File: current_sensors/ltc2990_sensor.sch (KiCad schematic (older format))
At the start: 14 parts

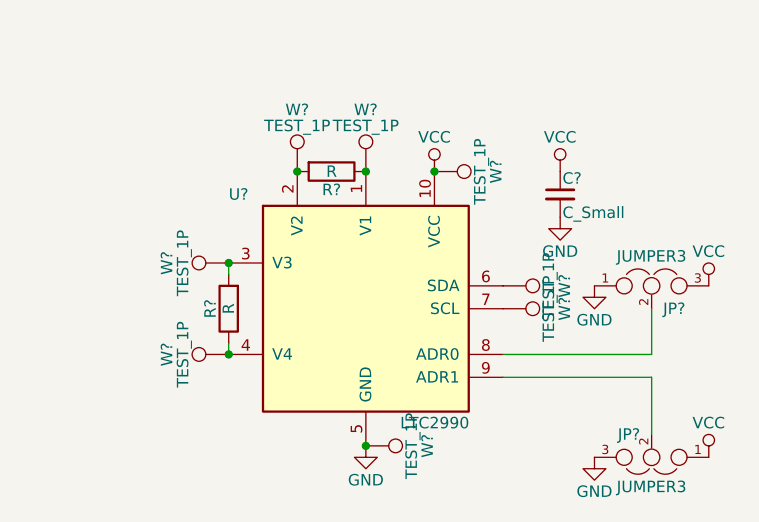
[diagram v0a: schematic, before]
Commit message: Made LTC2990 current sensor addon, untested
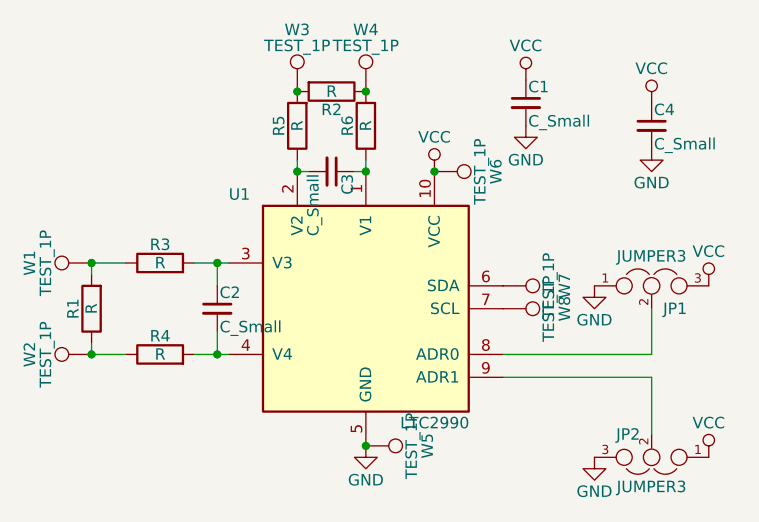
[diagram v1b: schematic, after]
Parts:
- added C2, C3, C4: C_Small, Capacitors_SMD:C_0603, symbol C_Small
- added R3, R4, R5, R6: R, Resistors_SMD:R_0603, symbol R
- C1: renamed from C?; footprint (none) -> Capacitors_SMD:C_0603
- JP1, JP2: renamed from JP?; footprint (none) -> Connect:GS3
- R1, R2: renamed from R?; footprint (none) -> Resistors_SMD:R_2512_HandSoldering
- U1: renamed from U?; footprint (none) -> Housings_SSOP:MSOP-10_3x3mm_Pitch0.5mm
- W1, W2, W3, W4: renamed from W?; footprint (none) -> Measurement_Points:Measurement_Point_Square-SMD-Pad_Big
- W5, W6, W7, W8: renamed from W?; footprint (none) -> Measurement_Points:Measurement_Point_Square-SMD-Pad_Small
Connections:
- net GND: now also C4.2
- net VCC: now also C4.1
- net at R2.1, W4.1: now also R6.2; no longer U1.1 (V1)
- net at R2.2, W3.1: now also R5.2; no longer U1.2 (V2)
- net at R1.2, W1.1: now also R3.1; no longer U1.3 (V3)
- net at R1.1, W2.1: now also R4.1; no longer U1.4 (V4)
- new net: C3.1, R6.1, U1.1 (V1)
- new net: C3.2, R5.1, U1.2 (V2)
- new net: C2.1, R3.2, U1.3 (V3)
- new net: C2.2, R4.2, U1.4 (V4)
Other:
- moved on the sheet: C1, R1, R2, W1, W2, W3, W4

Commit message: Added ground pads to current sensor
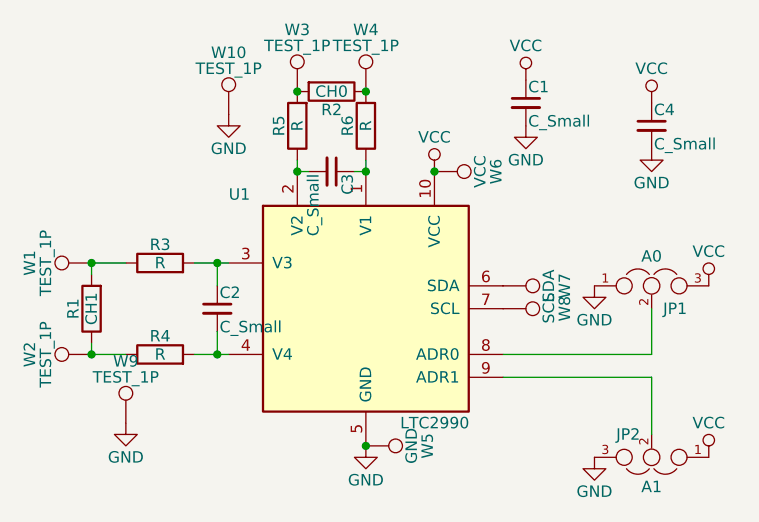
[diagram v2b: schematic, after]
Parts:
- added W10, W9: TEST_1P, Measurement_Points:Measurement_Point_Square-SMD-Pad_Big, symbol TEST_1P
- JP1: value JUMPER3 -> A0
- JP2: value JUMPER3 -> A1
- R1: value R -> CH1
- R2: value R -> CH0
- W5: value TEST_1P -> GND
- W6: value TEST_1P -> VCC
- W7: value TEST_1P -> SDA
- W8: value TEST_1P -> SCL
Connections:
- net GND: now also W10.1, W9.1
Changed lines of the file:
@@
 P 3200 2850
 F 0 "W7" H 3200 3120 50  0000 C CNN
-F 1 "TEST_1P" H 3200 3050 50  0000 C CNN
+F 1 "SDA" H 3200 3050 50  0000 C CNN
 F 2 "Measurement_Points:Measurement_Point_Square-SMD-Pad_Small" H 3400 2850 50  0001 C CNN
 F 3 "" H 3400 2850 50  0000 C CNN
@@
 P 2900 2350
 F 0 "W6" H 2900 2620 50  0000 C CNN
-F 1 "TEST_1P" H 2900 2550 50  0000 C CNN
+F 1 "VCC" H 2900 2550 50  0000 C CNN
 F 2 "Measurement_Points:Measurement_Point_Square-SMD-Pad_Small" H 3100 2350 50  0001 C CNN
 F 3 "" H 3100 2350 50  0000 C CNN
@@
 P 2600 3550
 F 0 "W5" H 2600 3820 50  0000 C CNN
-F 1 "TEST_1P" H 2600 3750 50  0000 C CNN
+F 1 "GND" H 2600 3750 50  0000 C CNN
 F 2 "Measurement_Points:Measurement_Point_Square-SMD-Pad_Small" H 2800 3550 50  0001 C CNN
 F 3 "" H 2800 3550 50  0000 C CNN
@@
 P 3200 2950
 F 0 "W8" H 3200 3220 50  0000 C CNN
-F 1 "TEST_1P" H 3200 3150 50  0000 C CNN
+F 1 "SCL" H 3200 3150 50  0000 C CNN
 F 2 "Measurement_Points:Measurement_Point_Square-SMD-Pad_Small" H 3400 2950 50  0001 C CNN
 F 3 "" H 3400 2950 50  0000 C CNN
@@
 P 3850 2850
 F 0 "JP1" H 3900 2750 50  0000 L CNN
-F 1 "JUMPER3" H 3850 2950 50  0000 C BNN
+F 1 "A0" H 3850 2950 50  0000 C BNN
 F 2 "Connect:GS3" H 3850 2850 50  0001 C CNN
 F 3 "" H 3850 2850 50  0000 C CNN
@@
 P 3850 3600
 F 0 "JP2" H 3900 3500 50  0000 L CNN
-F 1 "JUMPER3" H 3850 3700 50  0000 C BNN
+F 1 "A1" H 3850 3700 50  0000 C BNN
 F 2 "Connect:GS3" H 3850 3600 50  0001 C CNN
 F 3 "" H 3850 3600 50  0000 C CNN
@@
 P 2450 2000
 F 0 "R2" V 2530 2000 50  0000 C CNN
-F 1 "R" V 2450 2000 50  0000 C CNN
+F 1 "CH0" V 2450 2000 50  0000 C CNN
 F 2 "Resistors_SMD:R_2512_HandSoldering" V 2380 2000 50  0001 C CNN
 F 3 "" H 2450 2000 50  0000 C CNN
@@
 P 1400 2950
 F 0 "R1" V 1480 2950 50  0000 C CNN
-F 1 "R" V 1400 2950 50  0000 C CNN
+F 1 "CH1" V 1400 2950 50  0000 C CNN
 F 2 "Resistors_SMD:R_2512_HandSoldering" V 1330 2950 50  0001 C CNN
 F 3 "" H 1400 2950 50  0000 C CNN
@@
 	1    0    0    -1
 $EndComp
+$Comp
+L TEST_1P W10
+U 1 1 589B979D
+P 2000 2100
+F 0 "W10" H 2000 2370 50  0000 C CNN
+F 1 "TEST_1P" H 2000 2300 50  0000 C CNN
+F 2 "Measurement_Points:Measurement_Point_Square-SMD-Pad_Big" H 2200 2100 50  0001 C CNN
+F 3 "" H 2200 2100 50  0000 C CNN
+	1    2000 2100
+	1    0    0    -1
+$EndComp
+$Comp
+L GND #PWR011
+U 1 1 589B9B95
+P 2000 2100
+F 0 "#PWR011" H 2000 1850 50  0001 C CNN
+F 1 "GND" H 2000 1950 50  0000 C CNN
+F 2 "" H 2000 2100 50  0000 C CNN
+F 3 "" H 2000 2100 50  0000 C CNN
+	1    2000 2100
+	1    0    0    -1
+$EndComp
+$Comp
+L TEST_1P W9
+U 1 1 589B9C8D
+P 1550 3450
+F 0 "W9" H 1550 3720 50  0000 C CNN
+F 1 "TEST_1P" H 1550 3650 50  0000 C CNN
+F 2 "Measurement_Points:Measurement_Point_Square-SMD-Pad_Big" H 1750 3450 50  0001 C CNN
+F 3 "" H 1750 3450 50  0000 C CNN
+	1    1550 3450
+	1    0    0    -1
+$EndComp
+$Comp
+L GND #PWR012
+U 1 1 589B9D2E
+P 1550 3450
+F 0 "#PWR012" H 1550 3200 50  0001 C CNN
+F 1 "GND" H 1550 3300 50  0000 C CNN
+F 2 "" H 1550 3450 50  0000 C CNN
+F 3 "" H 1550 3450 50  0000 C CNN
+	1    1550 3450
+	1    0    0    -1
+$EndComp

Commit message: Redrawn the current sensor board
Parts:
- C1, C2, C3, C4: footprint Capacitors_SMD:C_0603 -> footprints:R_0603
- JP1, JP2: footprint Connect:GS3 -> footprints:GS3_SMALL
- R3, R4, R5, R6: footprint Resistors_SMD:R_0603 -> footprints:R_0603
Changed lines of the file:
@@
 F 0 "JP1" H 3900 2750 50  0000 L CNN
 F 1 "A0" H 3850 2950 50  0000 C BNN
-F 2 "Connect:GS3" H 3850 2850 50  0001 C CNN
+F 2 "footprints:GS3_SMALL" H 3850 2850 50  0001 C CNN
 F 3 "" H 3850 2850 50  0000 C CNN
 	1    3850 2850
@@
 F 0 "JP2" H 3900 3500 50  0000 L CNN
 F 1 "A1" H 3850 3700 50  0000 C BNN
-F 2 "Connect:GS3" H 3850 3600 50  0001 C CNN
+F 2 "footprints:GS3_SMALL" H 3850 3600 50  0001 C CNN
 F 3 "" H 3850 3600 50  0000 C CNN
 	1    3850 3600
@@
 F 0 "C1" H 3310 2120 50  0000 L CNN
 F 1 "C_Small" H 3310 1970 50  0000 L CNN
-F 2 "Capacitors_SMD:C_0603" H 3300 2050 50  0001 C CNN
+F 2 "footprints:R_0603" H 3300 2050 50  0001 C CNN
 F 3 "" H 3300 2050 50  0000 C CNN
 	1    3300 2050
@@
 F 0 "R3" V 1780 2750 50  0000 C CNN
 F 1 "R" V 1700 2750 50  0000 C CNN
-F 2 "Resistors_SMD:R_0603" V 1630 2750 50  0001 C CNN
+F 2 "footprints:R_0603" V 1630 2750 50  0001 C CNN
 F 3 "" H 1700 2750 50  0000 C CNN
 	1    1700 2750
@@
 F 0 "R4" V 1780 3150 50  0000 C CNN
 F 1 "R" V 1700 3150 50  0000 C CNN
-F 2 "Resistors_SMD:R_0603" V 1630 3150 50  0001 C CNN
+F 2 "footprints:R_0603" V 1630 3150 50  0001 C CNN
 F 3 "" H 1700 3150 50  0000 C CNN
 	1    1700 3150
@@
 F 0 "R5" V 2380 2150 50  0000 C CNN
 F 1 "R" V 2300 2150 50  0000 C CNN
-F 2 "Resistors_SMD:R_0603" V 2230 2150 50  0001 C CNN
+F 2 "footprints:R_0603" V 2230 2150 50  0001 C CNN
 F 3 "" H 2300 2150 50  0000 C CNN
 	1    2300 2150
@@
 F 0 "R6" V 2680 2150 50  0000 C CNN
 F 1 "R" V 2600 2150 50  0000 C CNN
-F 2 "Resistors_SMD:R_0603" V 2530 2150 50  0001 C CNN
+F 2 "footprints:R_0603" V 2530 2150 50  0001 C CNN
 F 3 "" H 2600 2150 50  0000 C CNN
 	1    2600 2150
@@
 F 0 "C2" H 1960 3020 50  0000 L CNN
 F 1 "C_Small" H 1960 2870 50  0000 L CNN
-F 2 "Capacitors_SMD:C_0603" H 1950 2950 50  0001 C CNN
+F 2 "footprints:R_0603" H 1950 2950 50  0001 C CNN
 F 3 "" H 1950 2950 50  0000 C CNN
 	1    1950 2950
@@
 F 0 "C3" H 2460 2420 50  0000 L CNN
 F 1 "C_Small" H 2460 2270 50  0000 L CNN
-F 2 "Capacitors_SMD:C_0603" H 2450 2350 50  0001 C CNN
+F 2 "footprints:R_0603" H 2450 2350 50  0001 C CNN
 F 3 "" H 2450 2350 50  0000 C CNN
 	1    2450 2350
@@
 F 0 "C4" H 3860 2220 50  0000 L CNN
 F 1 "C_Small" H 3860 2070 50  0000 L CNN
-F 2 "Capacitors_SMD:C_0603" H 3850 2150 50  0001 C CNN
+F 2 "footprints:R_0603" H 3850 2150 50  0001 C CNN
 F 3 "" H 3850 2150 50  0000 C CNN
 	1    3850 2150
